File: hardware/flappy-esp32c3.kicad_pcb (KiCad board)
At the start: 2 copper layers, 90 x 60 mm, 55 parts, among them J1 USB-C-Breakout 16P, J2 LiPo 1S 500 mAh, J3 OLED SSD1306 SPI, J4 Arcade-Taster, SW1 Ein/Aus, U1 ESP32-C3-WROOM-02-N4, U2 MCP73831-2-OT, U3 AP2112K-3.3

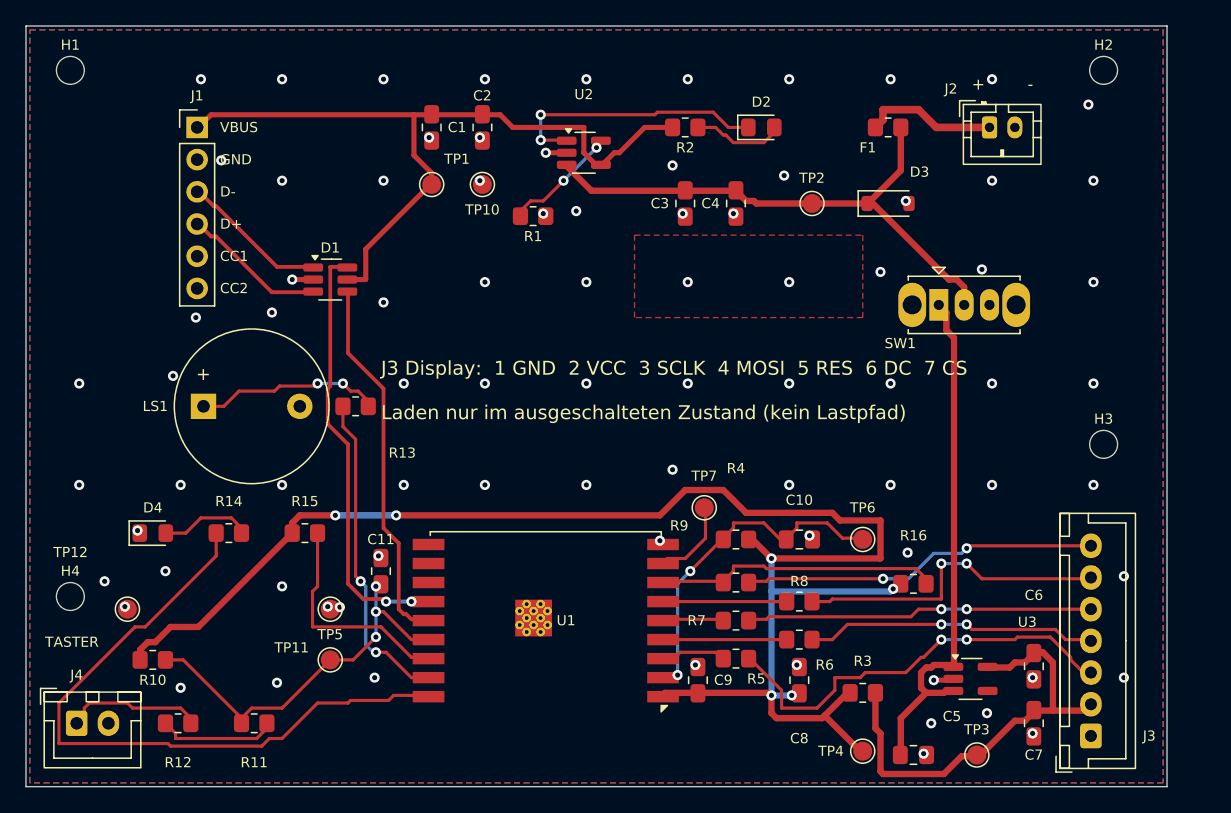
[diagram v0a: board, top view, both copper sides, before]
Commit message: Layout an den Schaltplan angleichen und auf 72 x 51 mm verkleinern
Abgleich Schaltplan <-> Layout
-----------------------------
Der Schaltplan war von Hand nachbearbeitet worden: R17/R18 (5k1) als
CC-Widerstaende an J1-5/J1-6. Weder gen/design.py noch die Platinendatei
kannten sie - die Platine haette keine CC-Widerstaende gehabt und mit einer
C-nach-C-Leitung kein VBUS bekommen.

R17/R18 stehen jetzt mit den Netzen CC1/CC2 in gen/design.py, J1-5 und J1-6
sind aus NO_CONNECT heraus. Sonst waren beide Dateien deckungsgleich.
Nach der Neuerzeugung: 0 Abweichungen (unabhaengig nachgerechnet).

Flaeche und Handbestueckbarkeit
-------------------------------
90 x 60 mm (5400 mm2) -> 72 x 51 mm (3672 mm2), 32 Prozent weniger.

Die alte Platine war zu 27 Prozent gefuellt und hatte trotzdem Stellen mit
0,15 mm Umrissabstand (LS1/R13, C9/R5, C9/U1, C8/R6) - der Platz lag als
leeres Band herum statt zwischen den Bauteilen. Jetzt gilt als pruefbare
Regel LOETABSTAND = 0,8 mm und RANDABSTAND = 0,5 mm; kleinster Wert im
Entwurf 0,82 mm. chk_place.py bricht ab, wenn es enger wird.

Leiterbahnen 843 -> 725 mm, Vias 113 -> 87, laengstes Rueckseitenstueck
10,8 -> 5,4 mm. C8 am Modulpin 10,8 -> 5,0 mm.

Weitere Befunde
---------------
* Die VBAT-Kuehlflaeche des Ladereglers lag nicht am Gehaeuse von U2,
  sondern nur ueber eine 0,5-mm-Bahn angebunden daneben - thermisch
  wirkungslos. Sie liegt jetzt unmittelbar am VBAT-Pad (122 mm2).
  chk_place.py prueft neu, dass jede NETZONE ein Pad ihres Netzes enthaelt;
  sonst wirft KiCad sie beim Fuellen als Insel wieder weg.
* Der Verdrahter reservierte nur fuer die eingeklemmten Masse-Mittelpins
  vorab ein Via. D1-5 (VBUS am ESD-Array) ist genauso eingeklemmt und fehlte.
  Liste heisst jetzt VORAB_VIA und nimmt den Netznamen aus der Netzliste.
* Die bauteil- und bahnfreien Flaechen unter Funkmodul und USB-C-Breakout
  waren als feste Koordinaten im Verdrahter verdrahtet. Sie werden jetzt aus
  der Platzierung abgeleitet und wandern beim Ve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
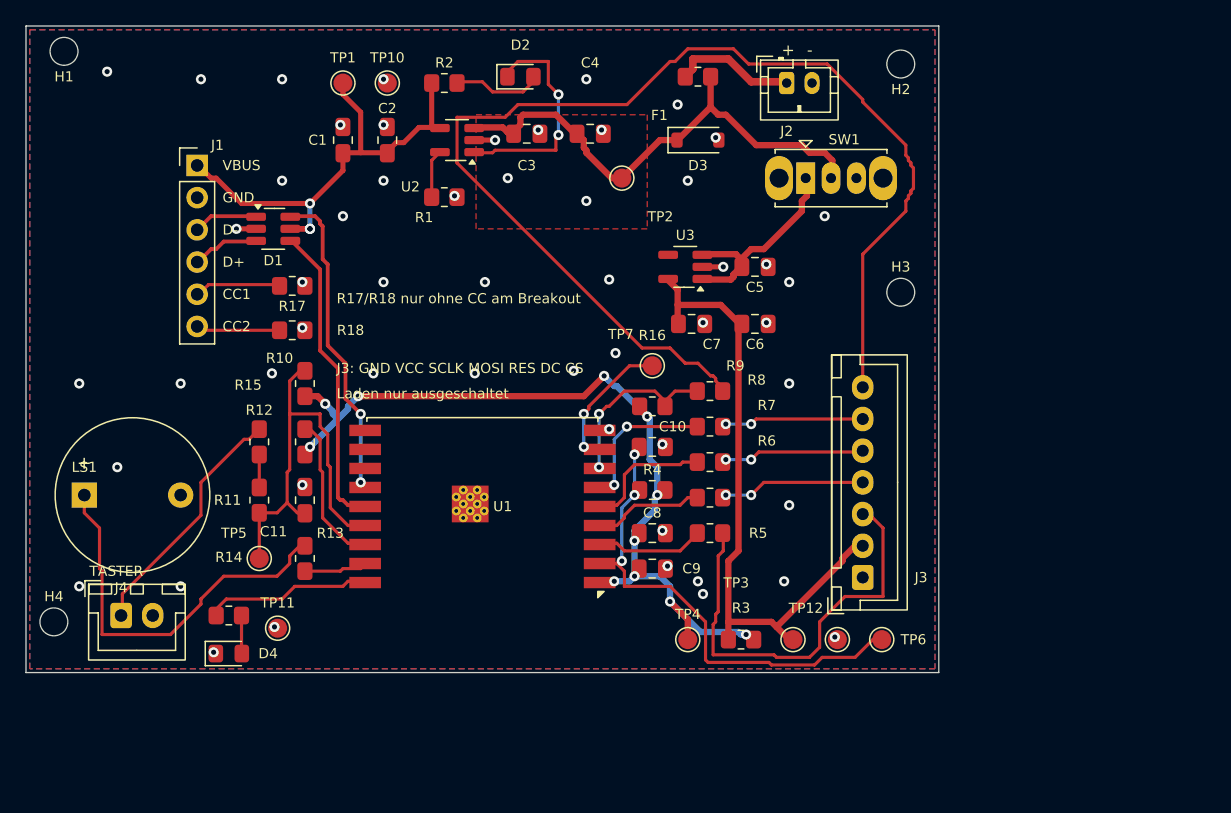
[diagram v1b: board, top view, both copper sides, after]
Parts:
- added R17: 5k1, Resistor_SMD:R_0805_2012Metric_Pad1.20x1.40mm_HandSolder, F.Cu at (51.0, 50.5)
- added R18: 5k1, Resistor_SMD:R_0805_2012Metric_Pad1.20x1.40mm_HandSolder, F.Cu at (51.0, 54.0)
- moved TP12 56.1 mm to (94.0, 78.4)
- moved C7 41.5 mm to (82.5, 53.5), turned to 0 degrees
- moved C5 40.5 mm to (87.5, 49.0)
- moved U3 39.5 mm to (82.0, 49.0), turned to 180 degrees
- moved C6 34.8 mm to (87.5, 53.5), turned to 0 degrees
- moved R16 24.9 mm to (79.4, 60.0)
- moved R10 24.9 mm to (52.0, 58.2), turned to 90 degrees
- moved R12 23.1 mm to (48.4, 62.8), turned to 90 degrees
- moved J3 21.9 mm to (96.0, 73.5)
- moved H3 20.0 mm to (99.0, 51.0)
- moved D2 19.4 mm to (69.0, 34.0)
- moved R2 19.3 mm to (63.0, 34.5)
- moved R11 17.6 mm to (48.4, 67.4), turned to 90 degrees
- moved TP3 17.1 mm to (90.5, 78.4)
- moved C8 16.4 mm to (79.4, 70.0), turned to 0 degrees
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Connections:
- J1 pad 5: unconnected-(J1-Pin_5-Pad5) -> CC1
- J1 pad 6: unconnected-(J1-Pin_6-Pad6) -> CC2
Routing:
- net OLED_CS: track 28.2 -> 94.1 mm, vias 2 -> 0
- net +3V3_MCU: track 125.1 -> 70.3 mm, vias 6 -> 11
- net LED_G: track 53.1 -> 13.1 mm
- net VBAT_SW: track 41.8 -> 16.4 mm
- net BUZZ: track 25.6 -> 5.05 mm, vias 2 -> 0
- net VBUS: track 59.0 -> 38.6 mm, vias 0 -> 3
- net BUZZ_P: track 14.7 -> 31.1 mm, vias 2 -> 0
- net OLED_RES: track 27.3 -> 11.3 mm
- net +3V3: track 35.1 -> 50.0 mm
- net OLED_DC: track 25.4 -> 11.2 mm
- net EN: track 27.0 -> 39.6 mm, vias 2 -> 3
- net MOSI: track 23.0 -> 11.5 mm
- net USB_DM: track 34.1 -> 25.1 mm
- net OLED_CS_MCU: track 22.3 -> 13.8 mm, vias 0 -> 2
- net BTN_CON: track 10.9 -> 19.3 mm
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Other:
- board size 90 x 60 mm -> 72 x 51 mm
- board text added: "FLAPPY BIRD ESP32-C3 REV. B"
- board text added: "J3: GND VCC SCLK MOSI RES DC CS"
- board text added: "Laden nur ausgeschaltet"
- board text added: "R17/R18 nur ohne CC am Breakout"
- board text removed: "FLAPPY BIRD ESP32-C3 REV. A"
- board text removed: "J3 Display: 1 GND 2 VCC 3 SCLK 4 MOSI 5 RES 6 DC 7 CS"
- board text removed: "Laden nur im ausgeschalteten Zustand (kein Lastpfad)"

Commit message: Pruefbericht nachgerechnet: Wert nach .sch, Pfade portabel, Repo aufgeraeumt
Nachgeprueft wurden die Befunde F1-F5 eines externen Berichts. F1, F2 und F3
sind berechtigt, F4 und F5 sind bereits dokumentierte Handlungspunkte, keine
Fehler. Die Messwerte des Berichts gehoeren zu Revision A (90 x 60 mm,
371 Bahnen) und stimmen bis auf zwei Abstaende, die von der Masseseite der
Kondensatoren gemessen wurden.

.sch als Master
---------------
Vollstaendiger Abgleich des erzeugten Schaltplans gegen die von Hand
gezeichnete Fassung auf main: 57 Bauteile, 41 Netze, gleiche Footprints,
gleiche Nichtanschluesse - genau eine Abweichung. R17/R18 hiessen von Hand
5.1k, in design.py 5k1. Der Schaltplan gewinnt: design.py sagt jetzt 5.1k.

Der Wertepruefer in tests.py kannte die Schreibweise mit Dezimalpunkt nicht
und haette 5.1k als unlesbar gemeldet. Er nimmt jetzt beide Formen (6k8 und
5.1k); _wert() rechnete schon vorher beide richtig um.

F2: feste macOS-Pfade
---------------------
erzeugen.sh, gen/design.py und gen/tests_stufe3.py hatten
/Applications/KiCad/... fest verdrahtet und brachen auf Linux und Windows ab.
Alle drei suchen jetzt selbst: eigene Umgebungsvariable, dann PATH bzw.
KICAD*_SYMBOL_DIR/KICAD*_FOOTPRINT_DIR, dann die ueblichen Installationsorte
von macOS, Linux und Windows. Notausgang sind FLAPPY_KICAD_CLI,
FLAPPY_KICAD_SYMBOLS und FLAPPY_KICAD_FOOTPRINTS. Findet erzeugen.sh kein
kicad-cli, bricht es gleich am Anfang ab statt auf halbem Weg.

F3: Git-Hygiene
---------------
.DS_Store (zwei Stueck) und _restore_backup_2026-08-25T08-33-44-858/ waren
getrackt, obwohl .DS_Store schon in .gitignore stand. Beide aus der
Versionsverwaltung genommen, _restore_backup_*/ ergaenzt. Das Backup enthielt
den Stand vor der Handaenderung (54 Bauteile, ohne R17/R18) und ist damit
inhaltlich ueberholt.

Nebenbei gefunden
-----------------
pruefbericht.md nannte fuer Revision A 8,1 % Rueckseitenanteil (69 mm von
860 mm). Nachgemessen an der eingecheckten Fassung sind es 8,4 % (7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
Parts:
- R17, R18: value 5k1 -> 5.1k
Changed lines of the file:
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@@
 			)
 		)
-		(property "Value" "5k1"
+		(property "Value" "5.1k"
 			(at 0 1.4 0)
 			(layer "F.Fab")
@@
 			)
 		)
-		(property "Value" "5k1"
+		(property "Value" "5.1k"
 			(at 0 1.4 0)
 			(layer "F.Fab")

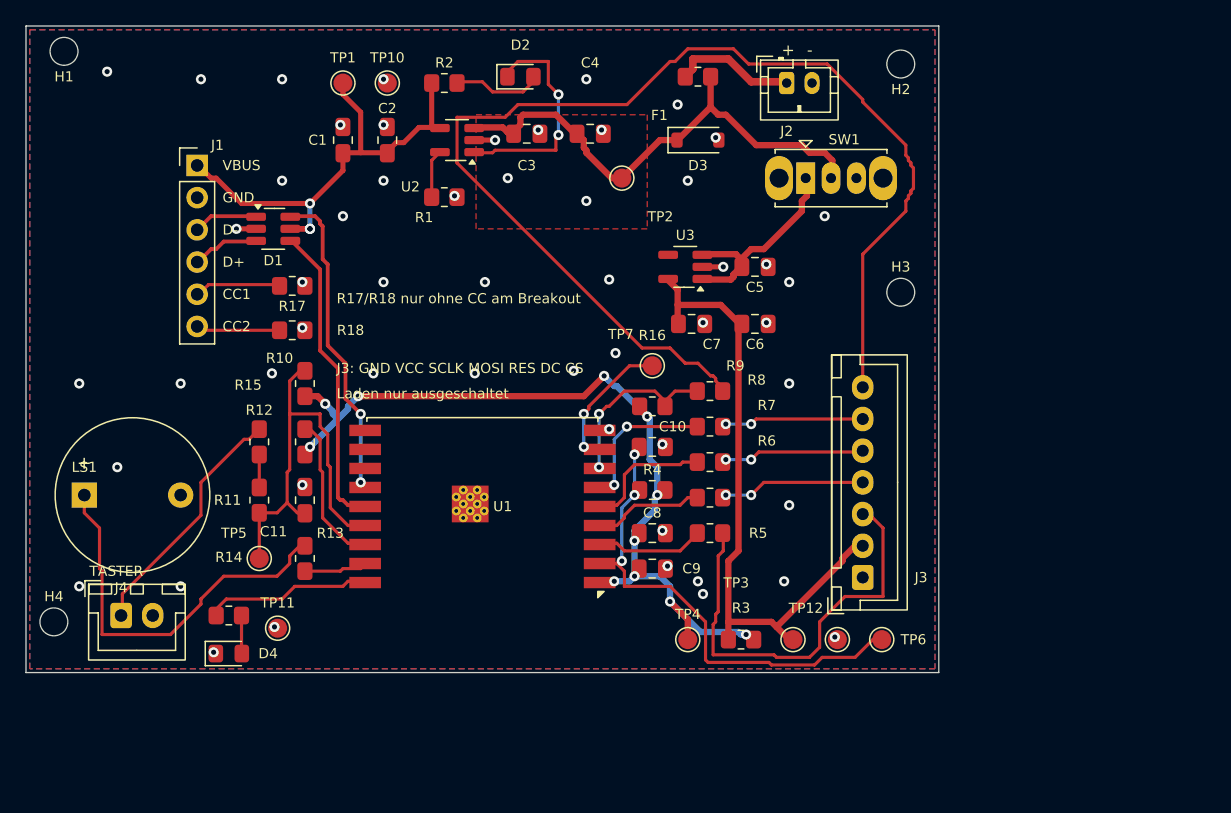
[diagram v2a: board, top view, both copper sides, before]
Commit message: Vierter Durchgang: DRC ohne KiCad nachgebaut, drei Fehler gefunden
Der dritte Durchgang liess ERC, DRC und die Fertigungsdaten offen, weil KiCad
in dieser Umgebung nicht zu bekommen ist. Dieser Durchgang baut nach, was
davon ohne KiCad pruefbar ist - und faellt dabei ueber drei echte Fehler.

1. Zwei Vias in derselben Bohrung
---------------------------------
Die im dritten Durchgang ergaenzte Vorabreservierung VORAB_VIA legt fuer den
eingeklemmten Mittelanschluss D1-5 eine Stichleitung samt Via. Danach verlegt
der Hauptlauf VBUS und faehrt denselben Weg noch einmal ab: ein Bahnstueck und
ein Via deckungsgleich obendrauf. Bohrung zu Bohrung -0,4 mm, ein
DRC-Verstoss, und die Bohrung stuende doppelt in der Excellon-Datei. Bei den
Massepins fiel das nie auf, weil GND nicht als Netz verlegt wird.
Behoben durch entdoppeln() in autoroute.py; zwei verschiedene Netze auf
derselben Bohrung brechen den Lauf ab, das waere ein Kurzschluss.

2. Bezeichner LS1 lag auf der Polaritaetsmarkierung des Piezo
-------------------------------------------------------------
mk_labels.py setzte eine Referenzbezeichnung ungeprueft auf den Festwert
(0, -2,2), wenn es keine freie Stelle fand - bei LS1 und J4 der Fall. Damit
lag "LS1" auf dem "+" des Buzzer-Footprints, die Polaritaet war auf dem
Bestueckungsdruck nicht mehr lesbar. Der Notfallzweig nimmt jetzt die Stelle
mit den wenigsten Ueberdeckungen, gewichtet Pads schwerer als Siebdrucklinien
und sucht weiter aussen. LS1 findet eine ganz freie Stelle, J4 kreuzt nur noch
eine Siebdrucklinie und meldet das.

3. Der Durchgang war ueberhaupt nicht geprueft
-----------------------------------------------
T6 prueft, dass verschiedene Netze sich nicht beruehren. Dass ein Netz nicht
auseinanderfaellt, prueffte nichts - das kam allein vom DRC, der nicht lief.
Neu ist T12: Beruehrungsgraph je Netz aus Bahnen, Vias und Pads, eine einzige
Insel gefordert. Netze an einer Kupferflaeche duerfen zerfallen, aber jede
Insel muss die Flaeche auf B.Cu ueber 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
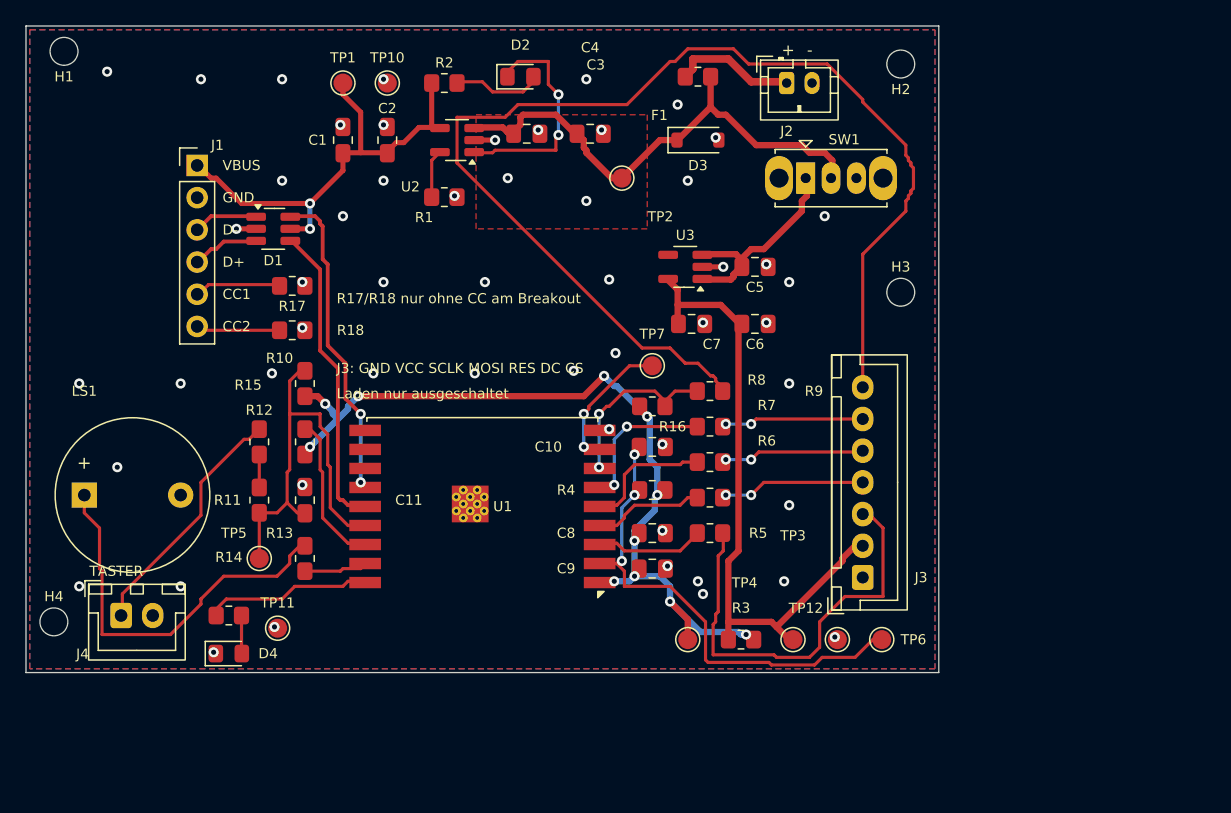
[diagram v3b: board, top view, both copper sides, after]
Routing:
- net VBUS: track 38.6 -> 37.0 mm, vias 3 -> 2
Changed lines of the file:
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@@
 		(tags "capacitor handsolder")
 		(property "Reference" "C10"
-			(at 1.6 -1.6 0)
+			(at -8.2 0.0 0)
 			(layer "F.SilkS")
 			(effects
@@
 		(tags "capacitor handsolder")
 		(property "Reference" "C11"
-			(at -2.48 -2.48 0)
+			(at 0.0 8.2 0)
 			(layer "F.SilkS")
 			(effects
@@
 		(tags "capacitor handsolder")
 		(property "Reference" "C3"
-			(at 0.0 2.5 0)
+			(at 5.44 -5.44 0)
 			(layer "F.SilkS")
 			(effects
@@
 		(tags "capacitor handsolder")
 		(property "Reference" "C4"
-			(at 0.0 -5.6 0)
+			(at 0.0 -6.8 0)
 			(layer "F.SilkS")
 			(effects
@@
 		(tags "capacitor handsolder")
 		(property "Reference" "C8"
-			(at 0.0 -1.6 0)
+			(at -6.8 0.0 0)
 			(layer "F.SilkS")
 			(effects
@@
 		(tags "capacitor handsolder")
 		(property "Reference" "C9"
-			(at 3.1 0.0 0)
+			(at -6.8 0.0 0)
 			(layer "F.SilkS")
 			(effects
@@
 		(tags "connector JST XH vertical")
 		(property "Reference" "J4"
-			(at 0.0 -2.2 0)
+			(at -3.04 3.04 0)
 			(layer "F.SilkS")
 			(effects
@@
 		(tags "buzzer")
 		(property "Reference" "LS1"
-			(at 0.0 -2.2 0)
+			(at 0.0 -8.2 0)
 			(layer "F.SilkS")
 			(effects
@@
 		(tags "resistor handsolder")
 		(property "Reference" "R13"
-			(at 2.0 2.0 0)
+			(at 2.0 -2.0 0)
 			(layer "F.SilkS")
 			(effects
@@
 		(tags "resistor handsolder")
 		(property "Reference" "R16"
-			(at 0.0 -5.6 0)
+			(at 1.6 1.6 0)
 			(layer "F.SilkS")
 			(effects
@@
 		(tags "resistor handsolder")
 		(property "Reference" "R4"
-			(at 0.0 -1.6 0)
+			(at -6.8 0.0 0)
 			(layer "F.SilkS")
 			(effects
@@
 		(tags "resistor handsolder")
 		(property "Reference" "R9"
-			(at 2.0 -2.0 0)
+			(at 8.2 0.0 0)
 			(layer "F.SilkS")
 			(effects
@@
 		(tags "test point SMD pad")
 		(property "Reference" "TP3"
-			(at -4.48 -4.48 0)
+			(at 0.0 -8.2 0)
 			(layer "F.SilkS")
 			(effects
@@
 		(tags "test point SMD pad")
 		(property "Reference" "TP4"
-			(at 0.0 -2.0 0)
+			(at 4.48 -4.48 0)
 			(layer "F.SilkS")
 			(effects
@@
 		(tags "test point SMD pad")
 		(property "Reference" "TP7"
-			(at -2.48 -2.48 0)
+			(at 0.0 -2.5 0)
 			(layer "F.SilkS")
 			(effects
@@
 	)
 	(segment
-		(start 52.4 46.0)
-		(end 50.8 46.0)
-		(width 0.4)
-		(layer "F.Cu")
-		(net 36)
-	)
-	(segment
 		(start 52.4 44.0)
 		(end 55.0 41.4)
@@
 		(size 0.8)
 		(drill 0.4)
-		(layers "F.Cu" "B.Cu")
-		(net 36)
-	)
-	(via
-		(at 52.4 46.0)
-		(size 0.8)
-		(drill 0.4)
